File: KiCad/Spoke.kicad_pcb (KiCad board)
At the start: 2 copper layers, 50 x 100 mm, 135 parts, among them J1 B2B-PH-K-S, J10 BL-A, J11 BL-C, J12 Amphenol 132289, J2 BAT+, J3 BAT-, J4 GCT USB4105/USB4110, J5 USB+, J6 USB-, J7 PLS-1x3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

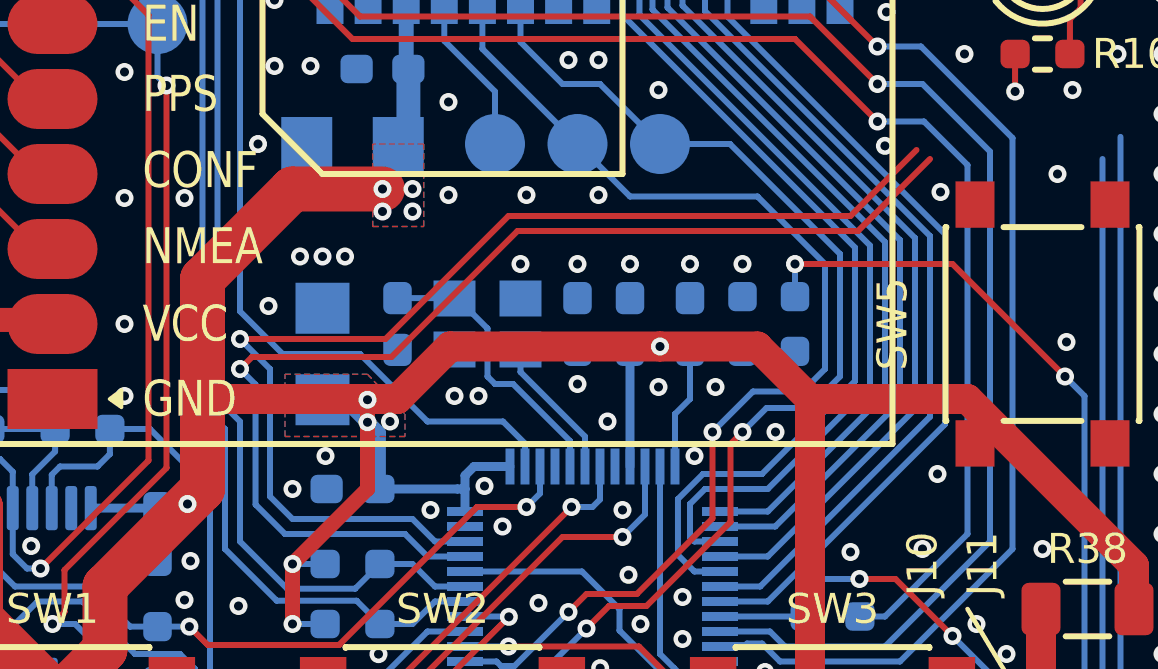
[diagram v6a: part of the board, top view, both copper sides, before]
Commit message: Route BTN_ALARM
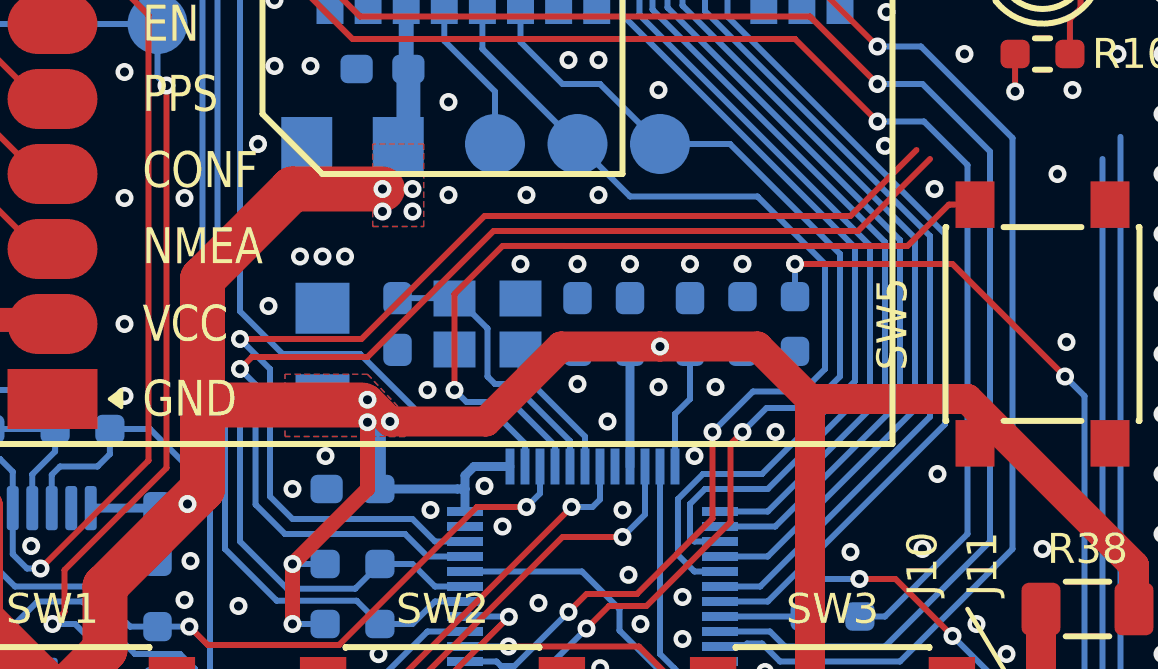
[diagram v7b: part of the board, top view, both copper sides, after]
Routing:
- net BTN_ALARM: track 0.00 -> 26.6 mm, vias 0 -> 1
- net +3V3: track 340.8 -> 340.3 mm
- net GND: vias 435 -> 434
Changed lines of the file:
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@@
 	)
 	(via
-		(at 100.4 88.4)
-		(size 0.6)
-		(drill 0.3)
-		(layers "F.Cu" "B.Cu")
-		(net 1)
-	)
-	(via
 		(at 76 114.5)
 		(size 0.6)
@@
 	)
 	(via
-		(at 116.6 81.6)
+		(at 116.4 81.5)
 		(size 0.6)
 		(drill 0.3)
@@
 	)
 	(via
+		(at 99.5 88.2)
+		(size 0.6)
+		(drill 0.3)
+		(layers "F.Cu" "B.Cu")
+		(free yes)
+		(net 1)
+	)
+	(via
 		(at 76 123)
 		(size 0.6)
@@
 	)
 	(via
-		(at 101.2 88.4)
-		(size 0.6)
-		(drill 0.3)
-		(layers "F.Cu" "B.Cu")
-		(free yes)
-		(net 1)
-	)
-	(via
 		(at 118 107.8)
 		(size 0.6)
@@
 	)
 	(segment
-		(start 98.5 88.5)
-		(end 92 88.5)
-		(width 1)
-		(layer "F.Cu")
-		(net 3)
-	)
-	(segment
 		(start 91.1125 113.8875)
 		(end 91 114)
@@
 	)
 	(segment
-		(start 82.5 73)
-		(end 82.5 66)
+		(start 103.95 86.75)
+		(end 107.25 86.75)
 		(width 1)
 		(layer "F.Cu")
@@
 	(segment
 		(start 82.5 73)
-		(end 78 77.5)
+		(end 82.5 66)
 		(width 1)
 		(layer "F.Cu")
@@
 	)
 	(segment
-		(start 97.525 88.5)
-		(end 97.5 88.525)
-		(width 0.5)
+		(start 82.5 73)
+		(end 78 77.5)
+		(width 1)
 		(layer "F.Cu")
 		(net 3)
@@
 	)
 	(segment
-		(start 98.5 88.5)
-		(end 100.25 86.75)
+		(start 92 88.7)
+		(end 92 91)
+		(width 1)
+		(layer "F.Cu")
+		(net 3)
+	)
+	(segment
+		(start 98.25 89.25)
+		(end 101.45 89.25)
 		(width 1)
 		(layer "F.Cu")
@@
 	)
 	(segment
+		(start 97.5 88.525)
+		(end 97.525 88.525)
+		(width 1)
+		(layer "F.Cu")
+		(net 3)
+	)
+	(segment
 		(start 110.4 105)
 		(end 104 105)
@@
 	)
 	(segment
+		(start 101.45 89.25)
+		(end 103.95 86.75)
+		(width 1)
+		(layer "F.Cu")
+		(net 3)
+	)
+	(segment
 		(start 93.5 114)
 		(end 91 114)
@@
 	)
 	(segment
-		(start 98.5 88.5)
-		(end 97.525 88.5)
-		(width 0.5)
-		(layer "F.Cu")
-		(net 3)
-	)
-	(segment
 		(start 91 114)
 		(end 88.75 114)
@@
 	)
 	(segment
-		(start 100.25 86.75)
-		(end 107.25 86.75)
-		(width 1)
-		(layer "F.Cu")
-		(net 3)
-	)
-	(segment
 		(start 112.25 103.15)
 		(end 110.4 105)
@@
 	)
 	(segment
+		(start 97.325 88.7)
+		(end 92 88.7)
+		(width 1.5)
+		(layer "F.Cu")
+		(net 3)
+	)
+	(segment
 		(start 97.25 114)
 		(end 97.25 121.75)
@@
 	)
 	(segment
-		(start 92 88.5)
-		(end 92 91)
+		(start 97.5 88.525)
+		(end 97.325 88.7)
 		(width 1)
 		(layer "F.Cu")
@@
 	)
 	(segment
+		(start 97.525 88.525)
+		(end 98.25 89.25)
+		(width 1)
+		(layer "F.Cu")
+		(net 3)
+	)
+	(segment
 		(start 110.5 86.75)
 		(end 107.25 86.75)
@@
 	)
 	(segment
-		(start 98.3 87.1)
-		(end 102.5 82.9)
+		(start 97.5 87.1)
+		(end 101.7 82.9)
 		(width 0.2)
 		(layer "F.Cu")
@@
 	)
 	(segment
-		(start 113.85 82.9)
-		(end 116.25 80.5)
+		(start 93.65 87.1)
+		(end 97.5 87.1)
 		(width 0.2)
 		(layer "F.Cu")
@@
 	)
 	(segment
-		(start 93.25 87.5)
-		(end 93.65 87.1)
+		(start 101.7 82.9)
+		(end 113.85 82.9)
 		(width 0.2)
 		(layer "F.Cu")
@@
 	)
 	(segment
-		(start 93.65 87.1)
-		(end 98.3 87.1)
+		(start 93.25 87.5)
+		(end 93.65 87.1)
 		(width 0.2)
 		(layer "F.Cu")
@@
 	)
 	(segment
-		(start 102.5 82.9)
-		(end 113.85 82.9)
+		(start 113.85 82.9)
+		(end 116.25 80.5)
 		(width 0.2)
 		(layer "F.Cu")
@@
 	)
 	(segment
-		(start 113.6 82.4)
-		(end 115.8 80.2)
+		(start 97.3 86.5)
+		(end 101.4 82.4)
 		(width 0.2)
 		(layer "F.Cu")
@@
 	(segment
 		(start 93.25 86.5)
-		(end 98.1 86.5)
+		(end 97.3 86.5)
 		(width 0.2)
 		(layer "F.Cu")
@@
 	)
 	(segment
-		(start 102.2 82.4)
+		(start 101.4 82.4)
 		(end 113.6 82.4)
 		(width 0.2)
@@
 	)
 	(segment
-		(start 98.1 86.5)
-		(end 102.2 82.4)
+		(start 113.6 82.4)
+		(end 115.8 80.2)
 		(width 0.2)
 		(layer "F.Cu")
@@
 		(net 120)
 	)
+	(segment
+		(start 104.1 83.4)
+		(end 115.5 83.4)
+		(width 0.2)
+		(layer "F.Cu")
+		(net 121)
+	)
+	(segment
+		(start 100.4 88.2)
+		(end 100.4 85)
+		(width 0.2)
+		(layer "F.Cu")
+		(net 121)
+	)
+	(segment
+		(start 104.099 83.399)
+		(end 104.1 83.4)
+		(width 0.2)
+		(layer "F.Cu")
+		(net 121)
+	)
+	(segment
+		(start 116.88 82.02)
+		(end 117.75 82.02)
+		(width 0.2)
+		(layer "F.Cu")
+		(net 121)
+	)
+	(segment
+		(start 115.5 83.4)
+		(end 116.88 82.02)
+		(width 0.2)
+		(layer "F.Cu")
+		(net 121)
+	)
+	(segment
+		(start 102.001 83.399)
+		(end 104.099 83.399)
+		(width 0.2)
+		(layer "F.Cu")
+		(net 121)
+	)
+	(segment
+		(start 100.4 85)
+		(end 102.001 83.399)
+		(width 0.2)
+		(layer "F.Cu")
+		(net 121)
+	)
+	(via
+		(at 100.4 88.2)
+		(size 0.6)
+		(drill 0.3)
+		(layers "F.Cu" "B.Cu")
+		(free yes)
+		(net 121)
+	)
+	(segment
+		(start 102.3 88.6)
+		(end 100.8 88.6)
+		(width 0.2)
+		(layer "B.Cu")
+		(net 121)
+	)
+	(segment
+		(start 103.75 90.75)
+		(end 103.75 90.05)
+		(width 0.2)
+		(layer "B.Cu")
+		(net 121)
+	)
+	(segment
+		(start 103.75 90.05)
+		(end 102.3 88.6)
+		(width 0.2)
+		(layer "B.Cu")
+		(net 121)
+	)
+	(segment
+		(start 100.8 88.6)
+		(end 100.4 88.2)
+		(width 0.2)
+		(layer "B.Cu")
+		(net 121)
+	)
 	(zone

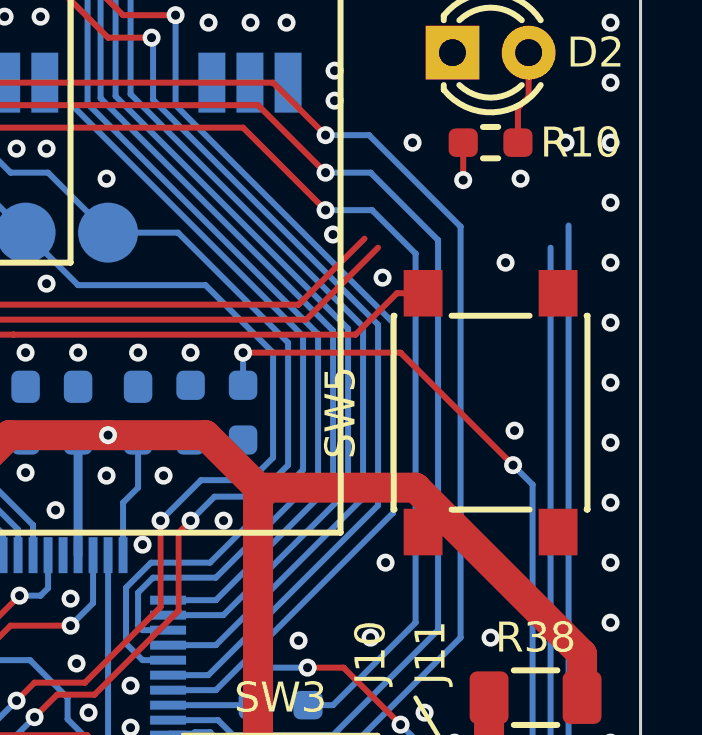
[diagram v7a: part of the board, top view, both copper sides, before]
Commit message: Set Alarm button position
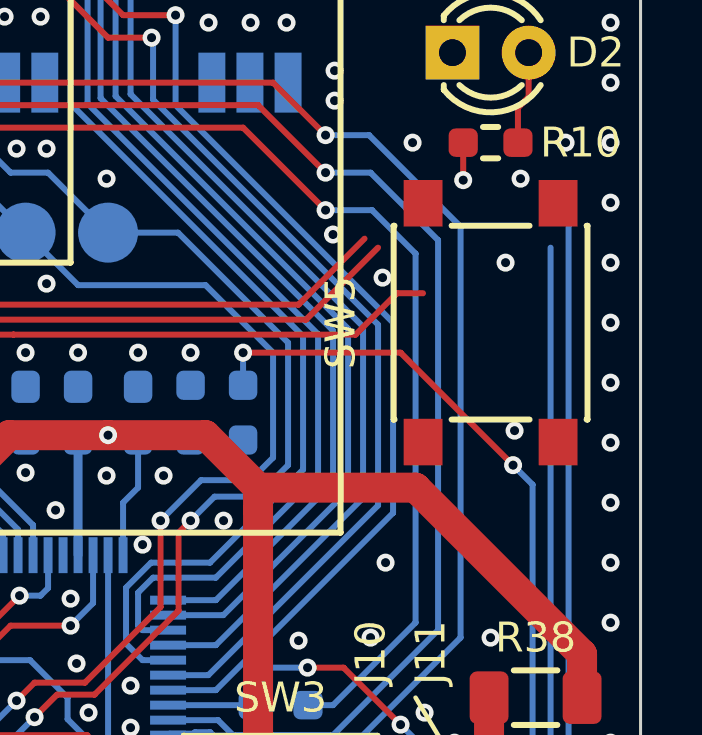
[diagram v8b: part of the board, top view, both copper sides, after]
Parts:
- moved SW5 3.00 mm to (120.0, 83.0)
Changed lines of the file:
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@@
 	(footprint "Spoke:Button_6x6"
 		(layer "F.Cu")
-		(at 120 86 90)
+		(at 120 83 90)
 		(property "Reference" "SW5"
 			(at 0 -5 90)
